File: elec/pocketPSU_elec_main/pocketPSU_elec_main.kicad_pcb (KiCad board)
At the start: 2 copper layers, 90 x 90 mm, 62 parts, among them J2 Conn_01x03_Pin, J3 Conn_01x12_Pin, SW1 EC11E09244BS, SW6 TS-1187A-B-A-B, U1 2N7002_C5224215, U2 ESP32-S3-WROOM-1(N16R2), U3 AMS1117-3.3, U4 FUSB302MPX, U5 F.0603.00026/P2-0603B1TS2-06T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

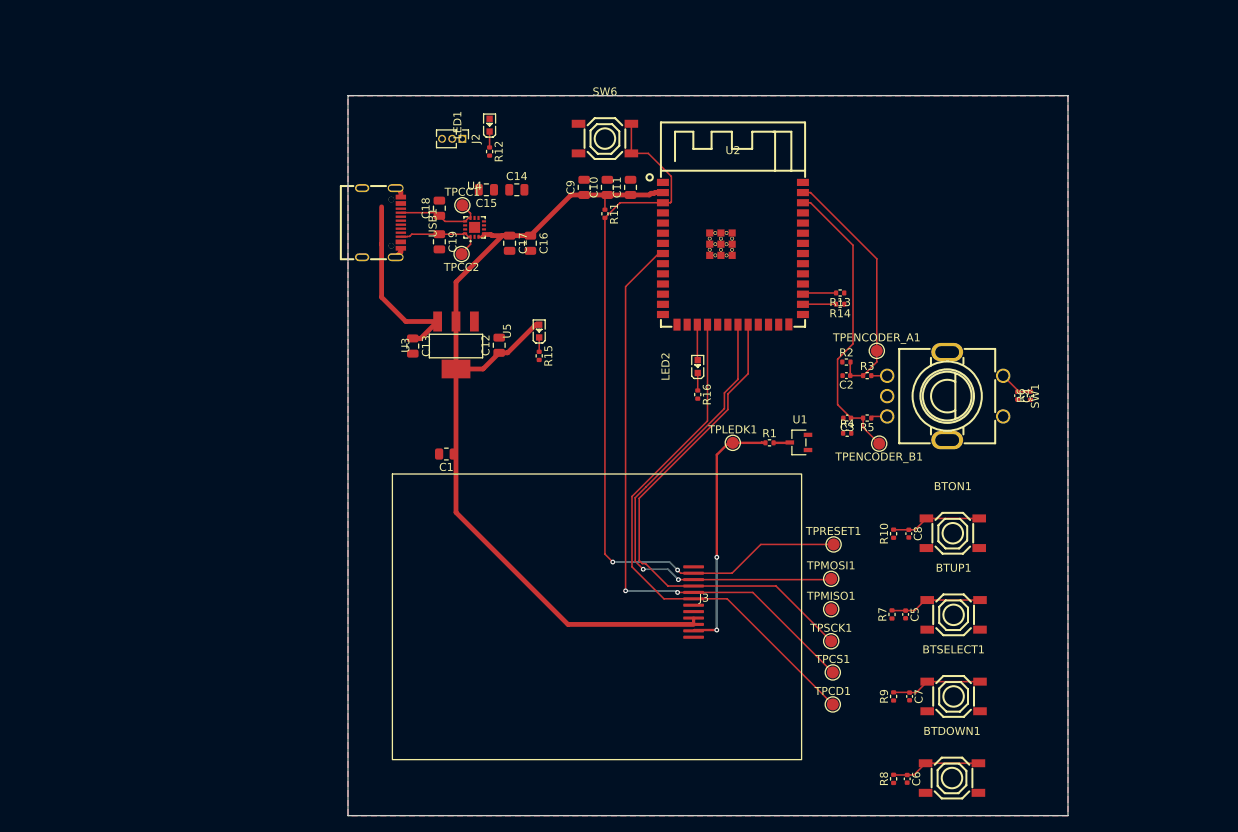
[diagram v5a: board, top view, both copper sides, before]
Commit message: route traces and add gnd pour
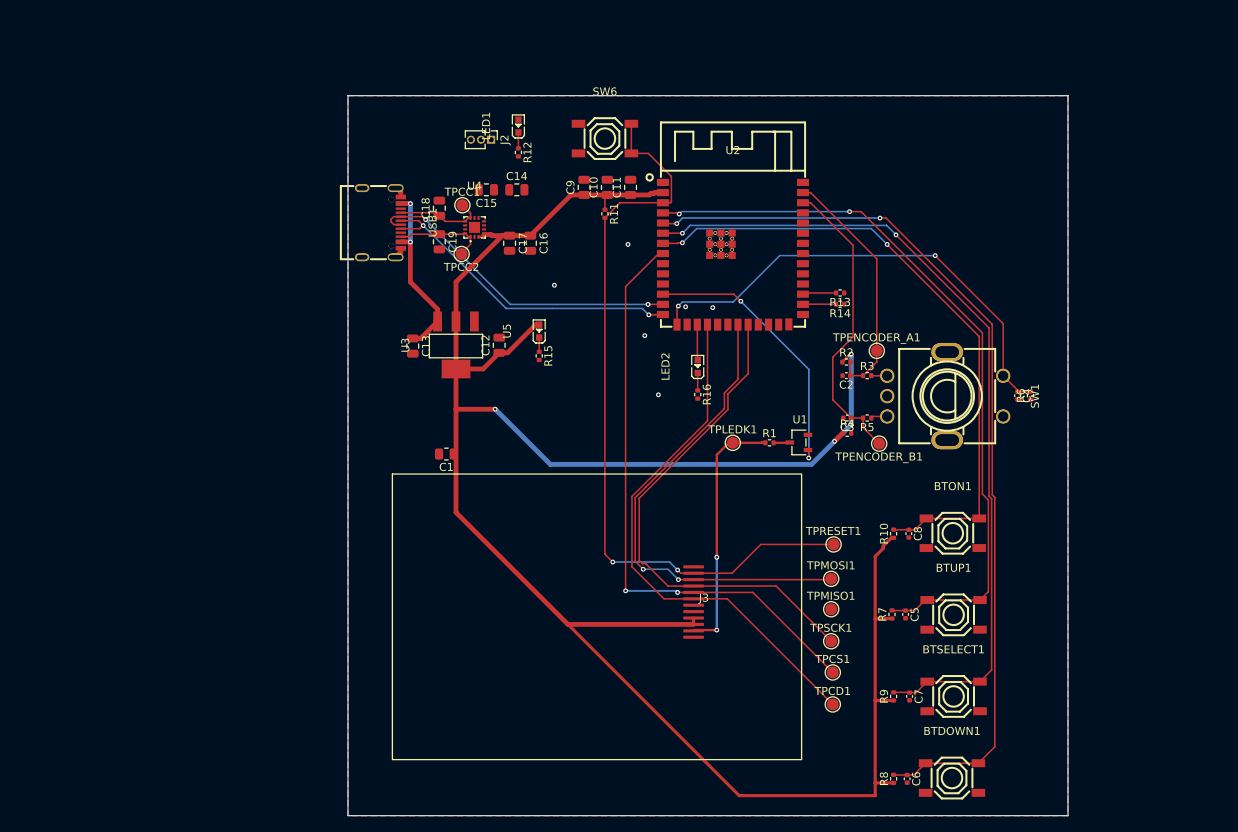
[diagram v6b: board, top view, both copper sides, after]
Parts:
- moved LED1 3.60 mm to (118.9, 39.5)
- moved R12 3.60 mm to (118.9, 42.8)
- moved J2 3.60 mm to (115.5, 41.2)
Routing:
- net +3.3V: track 113.4 -> 266.9 mm, vias 0 -> 3
- net /BT_2: track 11.2 -> 114.1 mm, vias 0 -> 2
- net /BT_3: track 11.4 -> 102.8 mm, vias 0 -> 2
- net /BT_1: track 11.6 -> 92.1 mm, vias 0 -> 2
- net /BT_4: track 11.3 -> 79.9 mm, vias 0 -> 2
- net /ENCODER_BT: track 4.36 -> 60.0 mm, vias 0 -> 2
- net /USB_DM: track 0.00 -> 40.7 mm, vias 0 -> 2
- net /USB_DP: track 0.00 -> 40.6 mm, vias 0 -> 2
- net /SCREEN_BACKLIGHT_EN: track 0.00 -> 34.3 mm, vias 0 -> 2
- net VBUS: track 23.5 -> 25.2 mm, vias 0 -> 2
- net GND: vias 0 -> 6

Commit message: add boot switch and test points
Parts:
- added J1: Conn_01x20_Pin, Connector_PinHeader_1.27mm:PinHeader_1x20_P1.27mm_Vertical, F.Cu at (184.3, 64.4)
- added R18: 10K, Resistor_SMD:R_0402_1005Metric, F.Cu at (156.5, 65.7)
- added SW3: TS-1187A-B-A-B, footprints:SW-SMD_4P-L5.1-W5.1-P3.70-LS6.5-TL-2, F.Cu at (152.7, 69.8)
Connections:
- U2 pad 10: unconnected-(U2-IO17-Pad10) -> /microcontroller/IO17
- U2 pad 11: unconnected-(U2-IO18-Pad11) -> /microcontroller/IO18
- U2 pad 16: unconnected-(U2-IO46-Pad16) -> /microcontroller/IO46
- U2 pad 19: unconnected-(U2-IO11-Pad19) -> /microcontroller/IO11
- U2 pad 23: unconnected-(U2-IO21-Pad23) -> /microcontroller/IO21
- U2 pad 24: unconnected-(U2-IO47-Pad24) -> /microcontroller/IO47
- U2 pad 25: unconnected-(U2-IO48-Pad25) -> /microcontroller/IO48
- U2 pad 26: unconnected-(U2-IO45-Pad26) -> /microcontroller/IO45
- U2 pad 27: unconnected-(U2-IO0-Pad27) -> Net-(SW3-B)
- U2 pad 31: unconnected-(U2-IO38-Pad31) -> /microcontroller/IO38
- U2 pad 32: unconnected-(U2-IO39-Pad32) -> /microcontroller/IO39
- U2 pad 33: unconnected-(U2-IO40-Pad33) -> /microcontroller/IO40
- U2 pad 34: unconnected-(U2-IO41-Pad34) -> /microcontroller/IO41
- U2 pad 35: unconnected-(U2-IO42-Pad35) -> /microcontroller/IO42
- U2 pad 36: unconnected-(U2-RXD0-Pad36) -> /microcontroller/RXD0
- U2 pad 37: unconnected-(U2-TXD0-Pad37) -> /microcontroller/TXD0
- U2 pad 9: unconnected-(U2-IO16-Pad9) -> /microcontroller/IO16

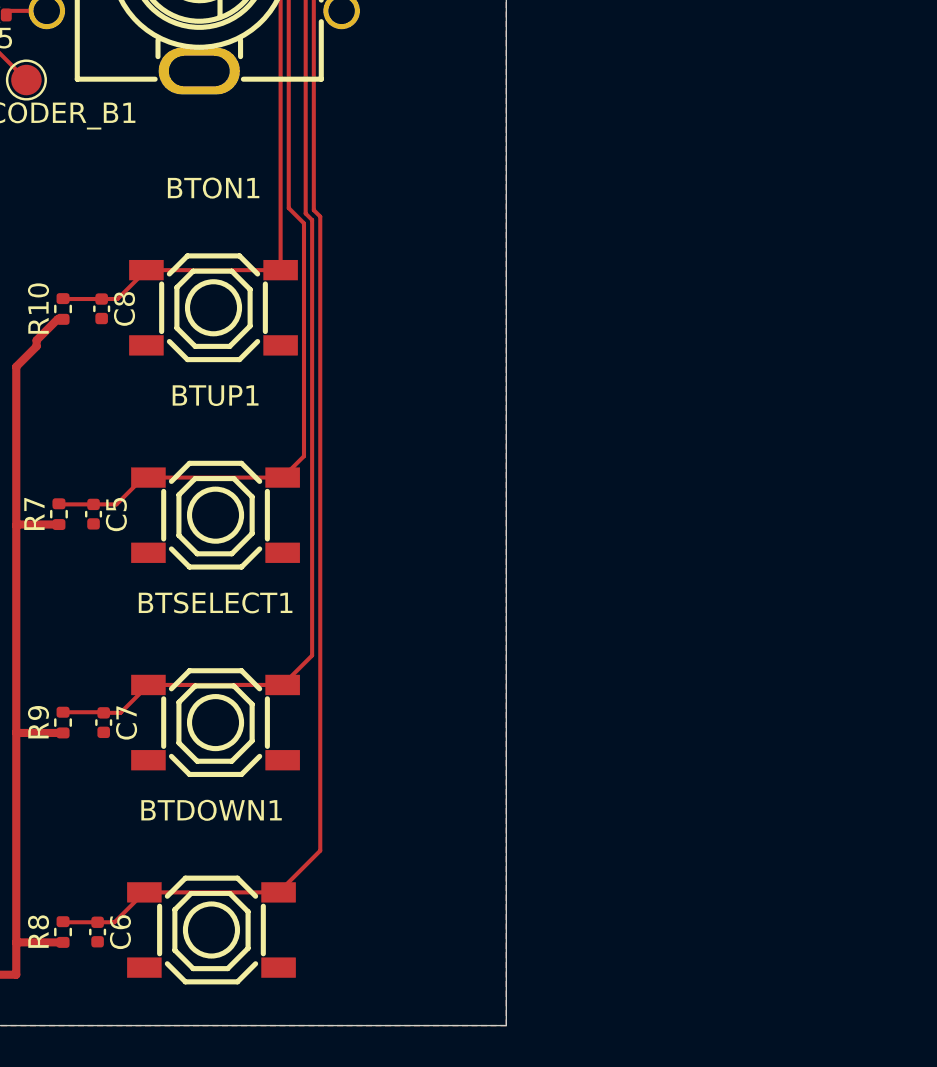
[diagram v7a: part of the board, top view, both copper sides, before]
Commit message: add buttons and leds for on/off indication
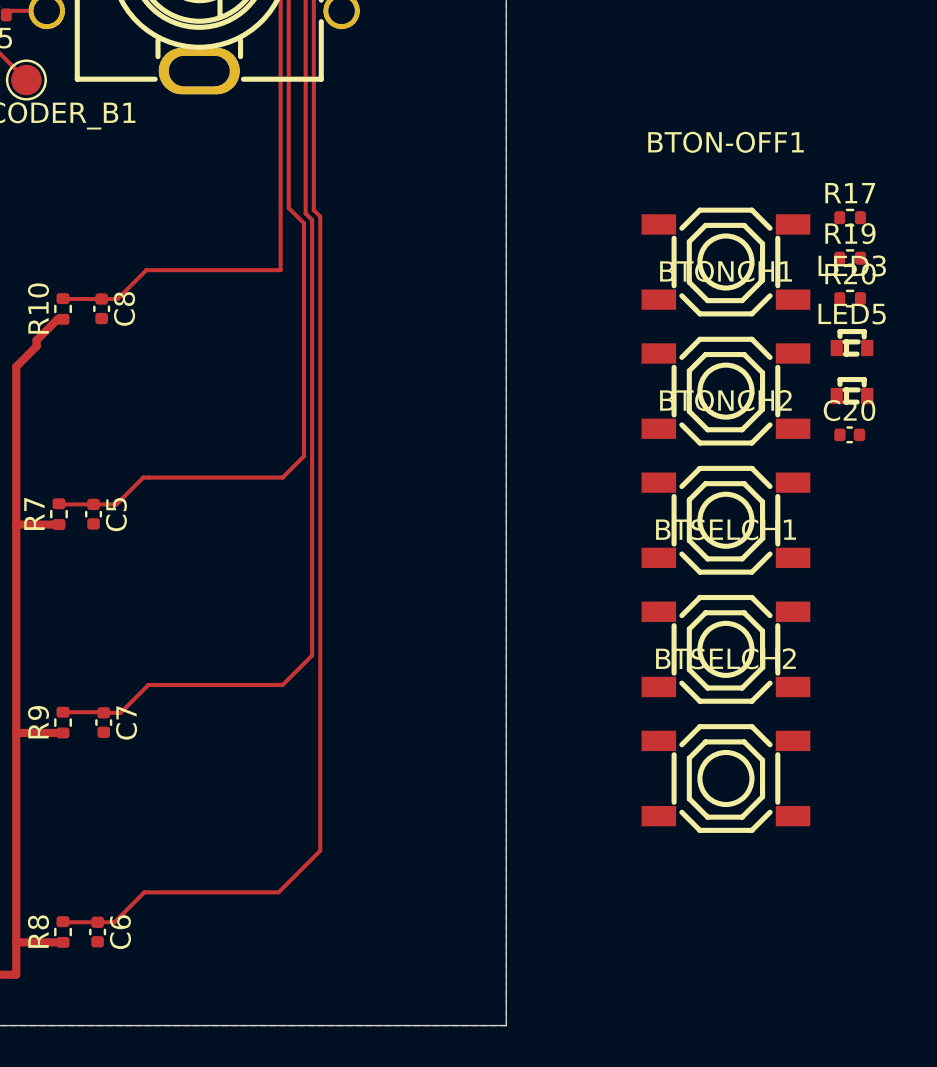
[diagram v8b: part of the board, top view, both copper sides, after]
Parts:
- removed BTDOWN1, BTON1, BTSELECT1, BTUP1: TS-1187A-B-A-B, footprints:SW-SMD_4P-L5.1-W5.1-P3.70-LS6.5-TL-2
- added BTON-OFF1: TS-1187A-B-A-B, footprints:SW-SMD_4P-L5.1-W5.1-P3.70-LS6.5-TL-2, F.Cu at (198.4, 88.2)
- added BTONCH1: TS-1187A-B-A-B, footprints:SW-SMD_4P-L5.1-W5.1-P3.70-LS6.5-TL-2, F.Cu at (198.4, 94.5)
- added BTONCH2: TS-1187A-B-A-B, footprints:SW-SMD_4P-L5.1-W5.1-P3.70-LS6.5-TL-2, F.Cu at (198.4, 100.8)
- added BTSELCH1: TS-1187A-B-A-B, footprints:SW-SMD_4P-L5.1-W5.1-P3.70-LS6.5-TL-2, F.Cu at (198.4, 107.2)
- added BTSELCH2: TS-1187A-B-A-B, footprints:SW-SMD_4P-L5.1-W5.1-P3.70-LS6.5-TL-2, F.Cu at (198.4, 113.5)
- added C20: 10nF, Capacitor_SMD:C_0402_1005Metric, F.Cu at (204.5, 96.7)
- added LED3: XL-1606SYGC, footprints:LED-SMD_L1.7-W1.1-RD_27-21, F.Cu at (204.6, 92.4)
- added LED5: XL-1606SYGC, footprints:LED-SMD_L1.7-W1.1-RD_27-21, F.Cu at (204.6, 94.7)
- added R17: 10K, Resistor_SMD:R_0402_1005Metric, F.Cu at (204.5, 86.0)
- added R19: 100R, Resistor_SMD:R_0402_1005Metric, F.Cu at (204.5, 88.0)
- added R20: 100R, Resistor_SMD:R_0402_1005Metric, F.Cu at (204.5, 90.0)
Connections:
- net /BT_1 renamed /microcontroller/BT_SEL_CH1
- net /BT_3 renamed /microcontroller/BT_SEL_CH2
- net /ENCODER_A renamed /microcontroller/ENCODER_A
- net /ENCODER_B renamed /microcontroller/ENCODER_B
- net /ENCODER_BT renamed /microcontroller/ENCODER_BT
- net /SCREEN_BACKLIGHT_EN renamed /user_interface/BACKLIGHT_EN
- net /SPI_CS renamed /user_interface/SPI_CS
- net /SPI_DC renamed /user_interface/SPI_DC
- net /SPI_MISO renamed /user_interface/SPI_MISO
- net /SPI_MOSI renamed /user_interface/SPI_MOSI
- net /SPI_RESET renamed /user_interface/SPI_RESET
- net /SPI_SCK renamed /user_interface/SPI_SCK
- C6 pad 1: /BT_2 -> /microcontroller/BT_ON_OFF
- C8 pad 1: /BT_4 -> /microcontroller/BT_ON_CH1
- J1 pad 1: /microcontroller/IO16 -> /microcontroller/IO17
- J1 pad 10: /microcontroller/IO42 -> /microcontroller/IO45
- J1 pad 11: /microcontroller/IO45 -> /microcontroller/IO46
- J1 pad 12: /microcontroller/IO46 -> /microcontroller/IO47
- J1 pad 13: /microcontroller/IO47 -> /microcontroller/IO48
- J1 pad 14: /microcontroller/IO48 -> /microcontroller/TXD0
- J1 pad 15: /microcontroller/TXD0 -> /microcontroller/RXD0
- J1 pad 16: /microcontroller/RXD0 -> unconnected-(J1-Pin_16-Pad16)
- J1 pad 2: /microcontroller/IO17 -> /microcontroller/IO18
- J1 pad 3: /microcontroller/IO18 -> /microcontroller/IO11
- J1 pad 4: /microcontroller/IO11 -> /microcontroller/IO21
- J1 pad 5: /microcontroller/IO21 -> /microcontroller/IO38
- J1 pad 6: /microcontroller/IO38 -> /microcontroller/IO39
- J1 pad 7: /microcontroller/IO39 -> /microcontroller/IO40
- J1 pad 8: /microcontroller/IO40 -> /microcontroller/IO41
- J1 pad 9: /microcontroller/IO41 -> /microcontroller/IO42
- R10 pad 2: /BT_4 -> /microcontroller/BT_ON_CH1
- R8 pad 2: /BT_2 -> /microcontroller/BT_ON_OFF
- U2 pad 10: /microcontroller/IO17 -> /microcontroller/CH1_LED
- U2 pad 11: /microcontroller/IO18 -> /microcontroller/CH2_LED
- U2 pad 5: /BT_2 -> /microcontroller/BT_ON_CH1
- U2 pad 7: /BT_4 -> /microcontroller/BT_ON_CH2
- U2 pad 9: /microcontroller/IO16 -> /microcontroller/BT_ON_OFF
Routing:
- net (no net): track 0.00 -> 194.0 mm, vias 0 -> 4
- net /BT_2: track 114.1 -> 0.00 mm, vias 2 -> 0
- net /BT_4: track 79.9 -> 0.00 mm, vias 2 -> 0
